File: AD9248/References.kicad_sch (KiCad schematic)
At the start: 0 parts

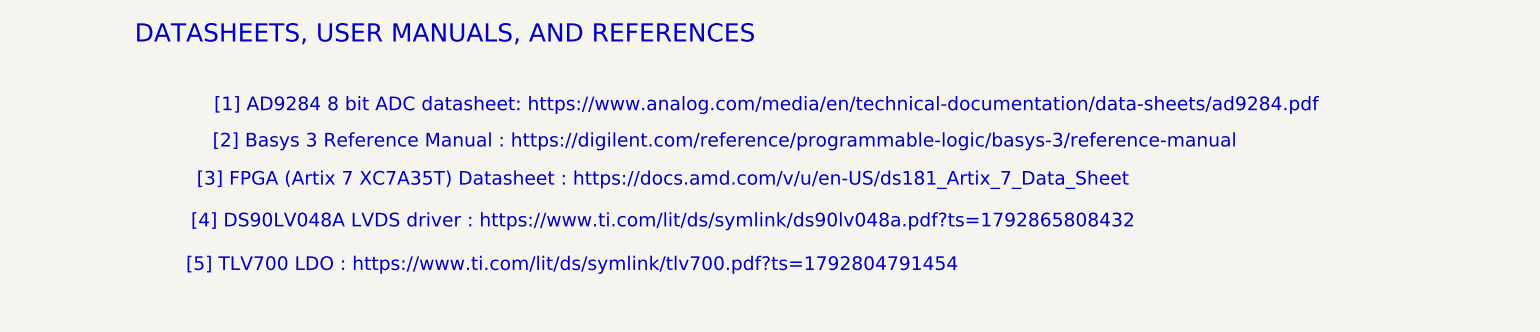
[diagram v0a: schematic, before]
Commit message: Rough draft completete, TODO: Cosmetic stuff (Make it more modular in schematic), simulate sallen key with non-ideal components, check FPGA pinout constraints for clock generation, validate design
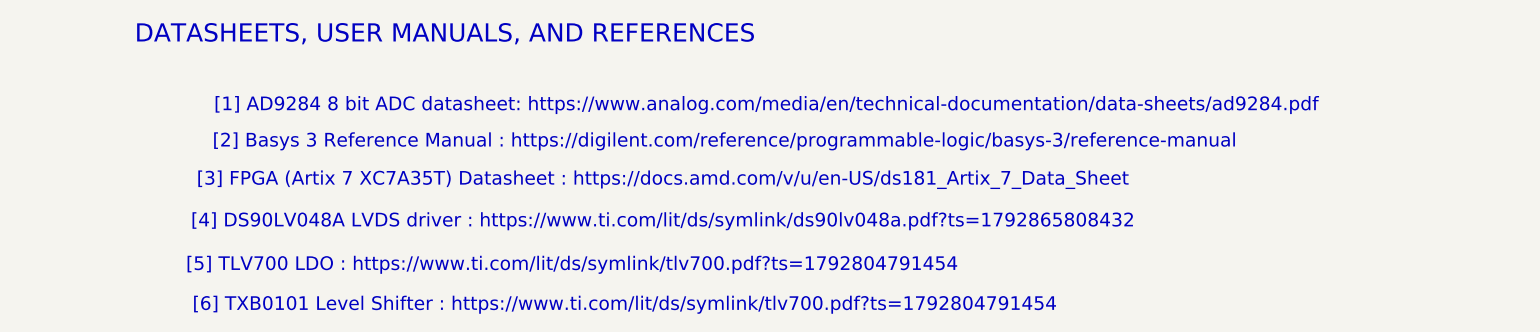
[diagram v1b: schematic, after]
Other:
- note added: "[6] TXB0101 Level Shifter : https://www.ti.com/lit/ds/symlink/tlv700.pdf?ts=1792804791454"
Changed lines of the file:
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@@
 	(generator_version "9.0")
 	(paper "A4")
+	(text "[6] TXB0101 Level Shifter : https://www.ti.com/lit/ds/symlink/tlv700.pdf?ts=1792804791454"
+		(exclude_from_sim no)
+		(at 89.662 58.928 0)
+		(effects
+			(font
+				(size 1.905 1.905)
+			)
+			(href "https://www.ti.com/lit/ds/symlink/tlv700.pdf?ts=1792804791454")
+		)
+	)
 	(text "DATASHEETS, USER MANUALS, AND REFERENCES"
 		(exclude_from_sim no)

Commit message: Finished and reviewed schematic, one change so far needs to be made: OE pin on level shifters must be externally toggled instead of tied to VCC. The IC requires VDDA/B to be fully ramped before pulling the OE high.
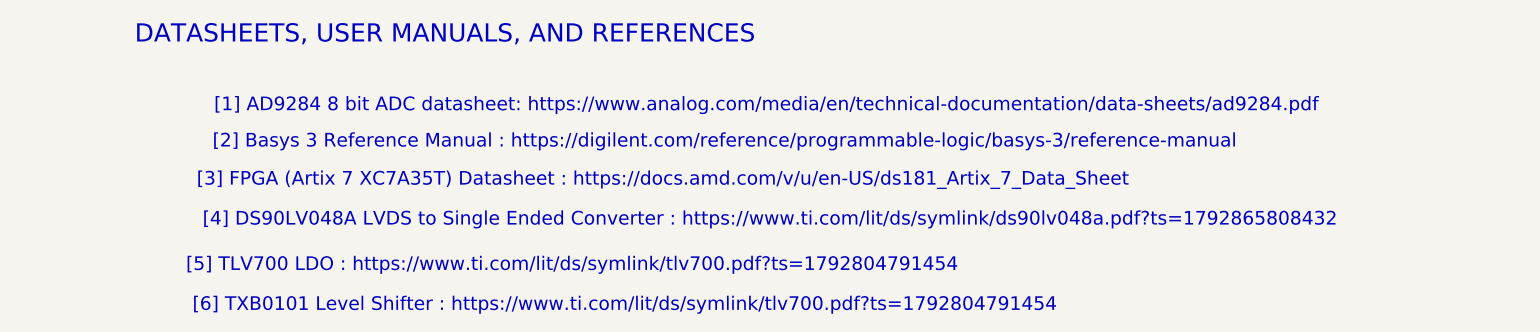
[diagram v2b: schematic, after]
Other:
- note added: "[4] DS90LV048A LVDS to Single Ended Converter : https://www.ti.com/lit/ds/symlink/ds90lv048a.pdf?ts=1792865808432"
- note removed: "[4] DS90LV048A LVDS driver : https://www.ti.com/lit/ds/symlink/ds90lv048a.pdf?ts=1792865808432"
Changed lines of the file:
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@@
 		)
 	)
-	(text "[4] DS90LV048A LVDS driver : https://www.ti.com/lit/ds/symlink/ds90lv048a.pdf?ts=1792865808432"
+	(text "[4] DS90LV048A LVDS to Single Ended Converter : https://www.ti.com/lit/ds/symlink/ds90lv048a.pdf?ts=1792865808432"
 		(exclude_from_sim no)
-		(at 94.996 47.244 0)
+		(at 109.982 46.99 0)
 		(effects
 			(font
